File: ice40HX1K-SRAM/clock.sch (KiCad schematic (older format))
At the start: 12 parts

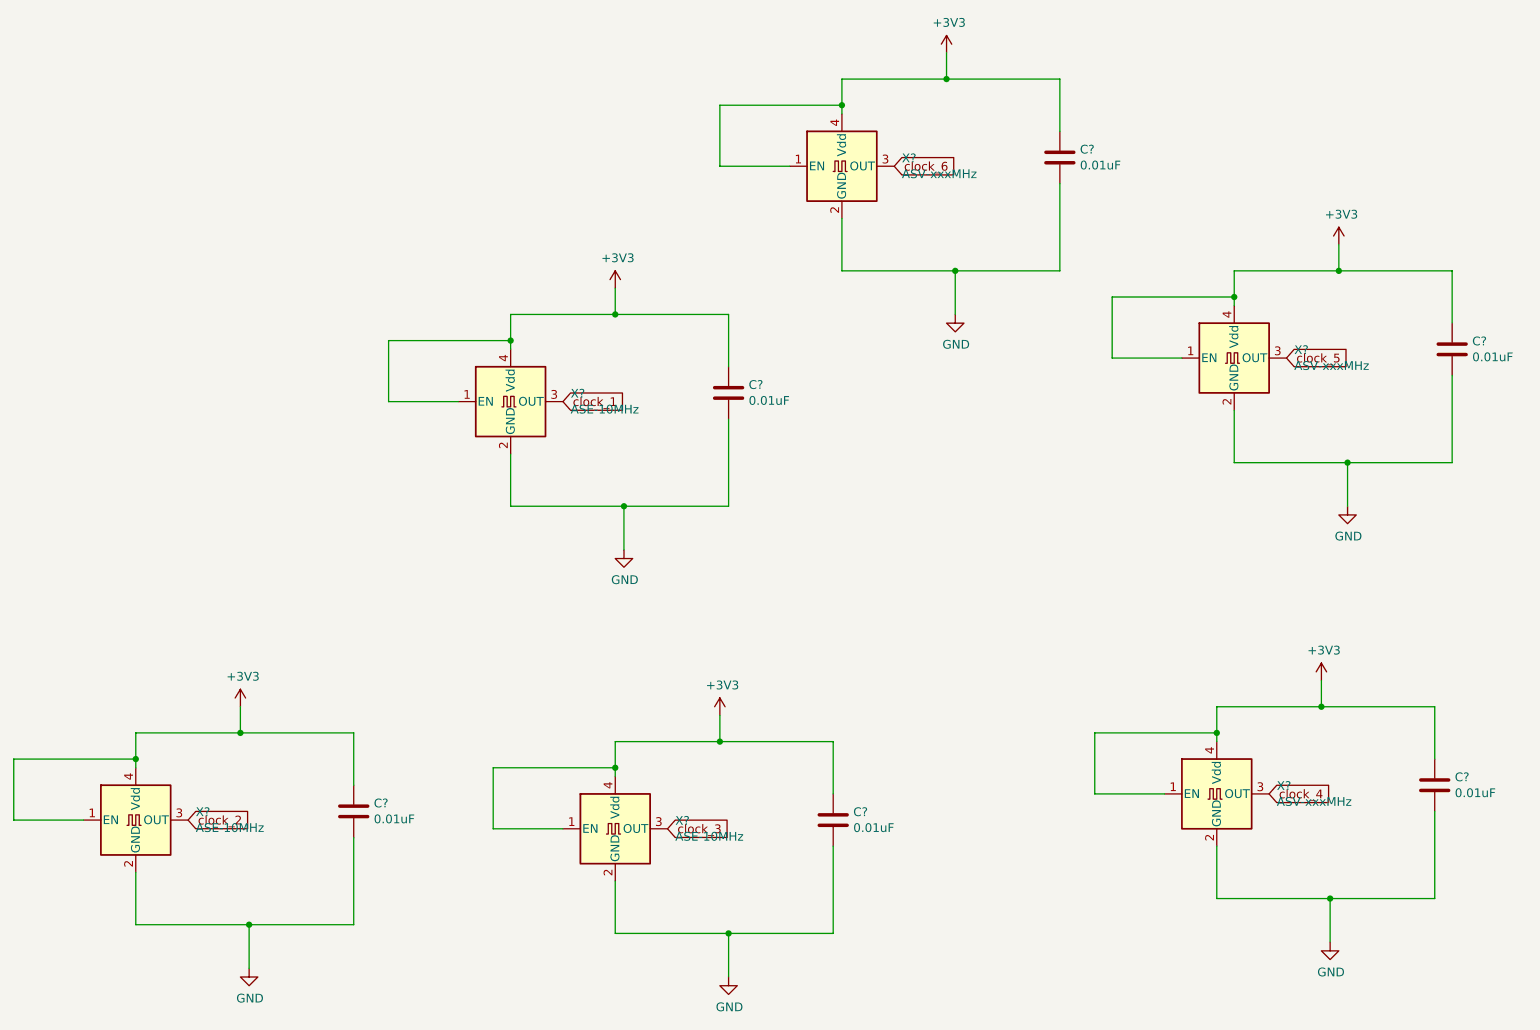
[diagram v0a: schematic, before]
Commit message: wiring FPGA nRF52 and ATSAMD11
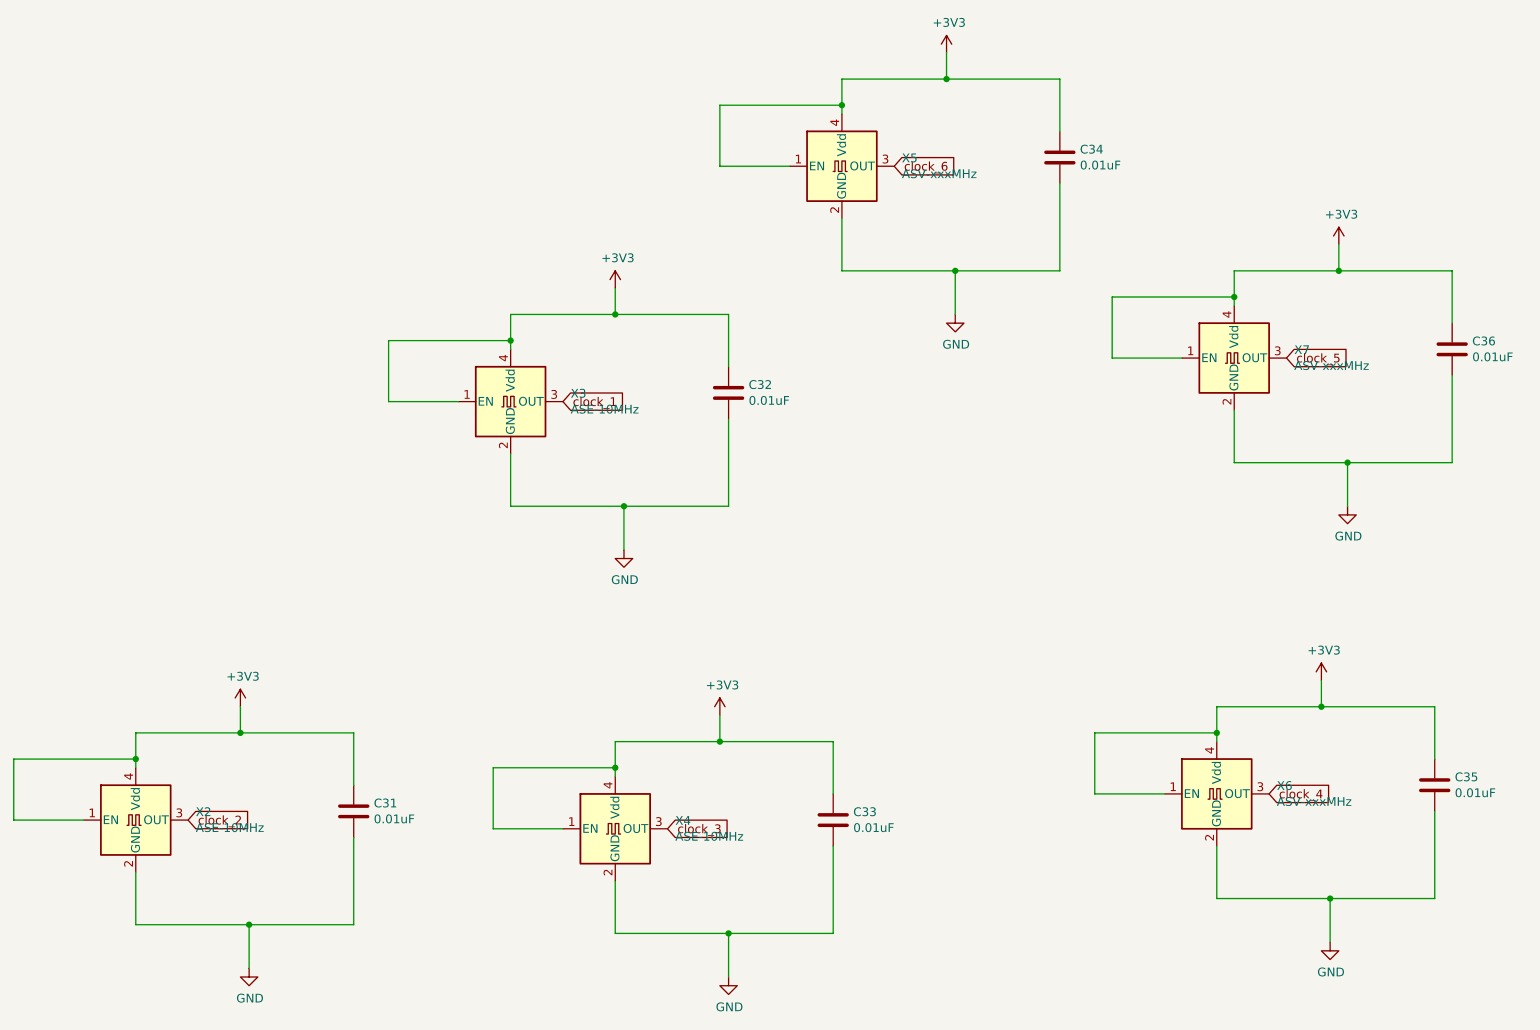
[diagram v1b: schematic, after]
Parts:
- gave numbers to parts that had none: 12
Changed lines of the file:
@@
 $EndDescr
 $Comp
-L Oscillator:ASE-xxxMHz X?
+L Oscillator:ASE-xxxMHz X3
 U 1 1 5E66FD40
 P 4050 2900
-F 0 "X?" H 4394 2946 50  0000 L CNN
+F 0 "X3" H 4394 2946 50  0000 L CNN
 F 1 "ASE-10MHz" H 4394 2855 50  0000 L CNN
 F 2 "Oscillator:Oscillator_SMD_Abracon_ASE-4Pin_3.2x2.5mm" H 4750 2550 50  0001 C CNN
@@
 $EndComp
 $Comp
-L Device:C C?
+L Device:C C32
 U 1 1 5E67058E
 P 5300 2850
-F 0 "C?" H 5415 2896 50  0000 L CNN
+F 0 "C32" H 5415 2896 50  0000 L CNN
 F 1 "0.01uF" H 5415 2805 50  0000 L CNN
 F 2 "" H 5338 2700 50  0001 C CNN
@@
 	5300 3500 5300 3000
 $Comp
-L power:+3V3 #PWR?
+L power:+3V3 #PWR072
 U 1 1 5E670EA7
 P 4650 2250
-F 0 "#PWR?" H 4650 2100 50  0001 C CNN
+F 0 "#PWR072" H 4650 2100 50  0001 C CNN
 F 1 "+3V3" H 4665 2423 50  0000 C CNN
 F 2 "" H 4650 2250 50  0001 C CNN
@@
 $EndComp
 $Comp
-L power:GND #PWR?
+L power:GND #PWR073
 U 1 1 5E67178D
 P 4700 3750
-F 0 "#PWR?" H 4700 3500 50  0001 C CNN
+F 0 "#PWR073" H 4700 3500 50  0001 C CNN
 F 1 "GND" H 4705 3577 50  0000 C CNN
 F 2 "" H 4700 3750 50  0001 C CNN
@@
 clock_1
 $Comp
-L Oscillator:ASV-xxxMHz X?
+L Oscillator:ASV-xxxMHz X7
 U 1 1 5E6438F8
 P 8200 2650
-F 0 "X?" H 8544 2696 50  0000 L CNN
+F 0 "X7" H 8544 2696 50  0000 L CNN
 F 1 "ASV-xxxMHz" H 8544 2605 50  0000 L CNN
 F 2 "Oscillator:Oscillator_SMD_Abracon_ASV-4Pin_7.0x5.1mm" H 8900 2300 50  0001 C CNN
@@
 $EndComp
 $Comp
-L Oscillator:ASE-xxxMHz X?
+L Oscillator:ASE-xxxMHz X2
 U 1 1 5E646F30
 P 1900 5300
-F 0 "X?" H 2244 5346 50  0000 L CNN
+F 0 "X2" H 2244 5346 50  0000 L CNN
 F 1 "ASE-10MHz" H 2244 5255 50  0000 L CNN
 F 2 "Oscillator:Oscillator_SMD_Abracon_ASE-4Pin_3.2x2.5mm" H 2600 4950 50  0001 C CNN
@@
 $EndComp
 $Comp
-L Device:C C?
+L Device:C C31
 U 1 1 5E646F36
 P 3150 5250
-F 0 "C?" H 3265 5296 50  0000 L CNN
+F 0 "C31" H 3265 5296 50  0000 L CNN
 F 1 "0.01uF" H 3265 5205 50  0000 L CNN
 F 2 "" H 3188 5100 50  0001 C CNN
@@
 	3150 5900 3150 5400
 $Comp
-L power:+3V3 #PWR?
+L power:+3V3 #PWR070
 U 1 1 5E646F42
 P 2500 4650
-F 0 "#PWR?" H 2500 4500 50  0001 C CNN
+F 0 "#PWR070" H 2500 4500 50  0001 C CNN
 F 1 "+3V3" H 2515 4823 50  0000 C CNN
 F 2 "" H 2500 4650 50  0001 C CNN
@@
 $EndComp
 $Comp
-L power:GND #PWR?
+L power:GND #PWR071
 U 1 1 5E646F48
 P 2550 6150
-F 0 "#PWR?" H 2550 5900 50  0001 C CNN
+F 0 "#PWR071" H 2550 5900 50  0001 C CNN
 F 1 "GND" H 2555 5977 50  0000 C CNN
 F 2 "" H 2550 6150 50  0001 C CNN
@@
 clock_2
 $Comp
-L Oscillator:ASE-xxxMHz X?
+L Oscillator:ASE-xxxMHz X4
 U 1 1 5E647806
 P 4650 5350
-F 0 "X?" H 4994 5396 50  0000 L CNN
+F 0 "X4" H 4994 5396 50  0000 L CNN
 F 1 "ASE-10MHz" H 4994 5305 50  0000 L CNN
 F 2 "Oscillator:Oscillator_SMD_Abracon_ASE-4Pin_3.2x2.5mm" H 5350 5000 50  0001 C CNN
@@
 $EndComp
 $Comp
-L Device:C C?
+L Device:C C33
 U 1 1 5E64780C
 P 5900 5300
-F 0 "C?" H 6015 5346 50  0000 L CNN
+F 0 "C33" H 6015 5346 50  0000 L CNN
 F 1 "0.01uF" H 6015 5255 50  0000 L CNN
 F 2 "" H 5938 5150 50  0001 C CNN
@@
 	5900 5950 5900 5450
 $Comp
-L power:+3V3 #PWR?
+L power:+3V3 #PWR074
 U 1 1 5E647818
 P 5250 4700
-F 0 "#PWR?" H 5250 4550 50  0001 C CNN
+F 0 "#PWR074" H 5250 4550 50  0001 C CNN
 F 1 "+3V3" H 5265 4873 50  0000 C CNN
 F 2 "" H 5250 4700 50  0001 C CNN
@@
 $EndComp
 $Comp
-L power:GND #PWR?
+L power:GND #PWR075
 U 1 1 5E64781E
 P 5300 6200
-F 0 "#PWR?" H 5300 5950 50  0001 C CNN
+F 0 "#PWR075" H 5300 5950 50  0001 C CNN
 F 1 "GND" H 5305 6027 50  0000 C CNN
 F 2 "" H 5300 6200 50  0001 C CNN
@@
 clock_3
 $Comp
-L Device:C C?
+L Device:C C36
 U 1 1 5E6489E3
 P 9450 2600
-F 0 "C?" H 9565 2646 50  0000 L CNN
+F 0 "C36" H 9565 2646 50  0000 L CNN
 F 1 "0.01uF" H 9565 2555 50  0000 L CNN
 F 2 "" H 9488 2450 50  0001 C CNN
@@
 	9450 3250 9450 2750
 $Comp
-L power:+3V3 #PWR?
+L power:+3V3 #PWR080
 U 1 1 5E6489EF
 P 8800 2000
-F 0 "#PWR?" H 8800 1850 50  0001 C CNN
+F 0 "#PWR080" H 8800 1850 50  0001 C CNN
 F 1 "+3V3" H 8815 2173 50  0000 C CNN
 F 2 "" H 8800 2000 50  0001 C CNN
@@
 $EndComp
 $Comp
-L power:GND #PWR?
+L power:GND #PWR081
 U 1 1 5E6489F5
 P 8850 3500
-F 0 "#PWR?" H 8850 3250 50  0001 C CNN
+F 0 "#PWR081" H 8850 3250 50  0001 C CNN
 F 1 "GND" H 8855 3327 50  0000 C CNN
 F 2 "" H 8850 3500 50  0001 C CNN
@@
 clock_5
 $Comp
-L Oscillator:ASV-xxxMHz X?
+L Oscillator:ASV-xxxMHz X6
 U 1 1 5E64DEA5
 P 8100 5150
-F 0 "X?" H 8444 5196 50  0000 L CNN
+F 0 "X6" H 8444 5196 50  0000 L CNN
 F 1 "ASV-xxxMHz" H 8444 5105 50  0000 L CNN
 F 2 "Oscillator:Oscillator_SMD_Abracon_ASV-4Pin_7.0x5.1mm" H 8800 4800 50  0001 C CNN
@@
 $EndComp
 $Comp
-L Device:C C?
+L Device:C C35
 U 1 1 5E64DEAB
 P 9350 5100
-F 0 "C?" H 9465 5146 50  0000 L CNN
+F 0 "C35" H 9465 5146 50  0000 L CNN
 F 1 "0.01uF" H 9465 5055 50  0000 L CNN
 F 2 "" H 9388 4950 50  0001 C CNN
@@
 	9350 5750 9350 5250
 $Comp
-L power:+3V3 #PWR?
+L power:+3V3 #PWR078
 U 1 1 5E64DEB7
 P 8700 4500
-F 0 "#PWR?" H 8700 4350 50  0001 C CNN
+F 0 "#PWR078" H 8700 4350 50  0001 C CNN
 F 1 "+3V3" H 8715 4673 50  0000 C CNN
 F 2 "" H 8700 4500 50  0001 C CNN
@@
 $EndComp
 $Comp
-L power:GND #PWR?
+L power:GND #PWR079
 U 1 1 5E64DEBD
 P 8750 6000
-F 0 "#PWR?" H 8750 5750 50  0001 C CNN
+F 0 "#PWR079" H 8750 5750 50  0001 C CNN
 F 1 "GND" H 8755 5827 50  0000 C CNN
 F 2 "" H 8750 6000 50  0001 C CNN
@@
 clock_4
 $Comp
-L Oscillator:ASV-xxxMHz X?
+L Oscillator:ASV-xxxMHz X5
 U 1 1 5E64FFD0
 P 5950 1550
-F 0 "X?" H 6294 1596 50  0000 L CNN
+F 0 "X5" H 6294 1596 50  0000 L CNN
 F 1 "ASV-xxxMHz" H 6294 1505 50  0000 L CNN
 F 2 "Oscillator:Oscillator_SMD_Abracon_ASV-4Pin_7.0x5.1mm" H 6650 1200 50  0001 C CNN
@@
 $EndComp
 $Comp
-L Device:C C?
+L Device:C C34
 U 1 1 5E64FFD6
 P 7200 1500
-F 0 "C?" H 7315 1546 50  0000 L CNN
+F 0 "C34" H 7315 1546 50  0000 L CNN
 F 1 "0.01uF" H 7315 1455 50  0000 L CNN
 F 2 "" H 7238 1350 50  0001 C CNN
@@
 	7200 2150 7200 1650
 $Comp
-L power:+3V3 #PWR?
+L power:+3V3 #PWR076
 U 1 1 5E64FFE2
 P 6550 900
-F 0 "#PWR?" H 6550 750 50  0001 C CNN
+F 0 "#PWR076" H 6550 750 50  0001 C CNN
 F 1 "+3V3" H 6565 1073 50  0000 C CNN
 F 2 "" H 6550 900 50  0001 C CNN
@@
 $EndComp
 $Comp
-L power:GND #PWR?
+L power:GND #PWR077
 U 1 1 5E64FFE8
 P 6600 2400
-F 0 "#PWR?" H 6600 2150 50  0001 C CNN
+F 0 "#PWR077" H 6600 2150 50  0001 C CNN
 F 1 "GND" H 6605 2227 50  0000 C CNN
 F 2 "" H 6600 2400 50  0001 C CNN

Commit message: wiring FPGA
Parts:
- C31, C32, C33, C34, C35, C36: footprint (none) -> Capacitor_SMD:C_0402_1005Metric
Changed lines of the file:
@@
 F 0 "C32" H 5415 2896 50  0000 L CNN
 F 1 "0.01uF" H 5415 2805 50  0000 L CNN
-F 2 "" H 5338 2700 50  0001 C CNN
+F 2 "Capacitor_SMD:C_0402_1005Metric" H 5338 2700 50  0001 C CNN
 F 3 "~" H 5300 2850 50  0001 C CNN
 	1    5300 2850
@@
 F 0 "C31" H 3265 5296 50  0000 L CNN
 F 1 "0.01uF" H 3265 5205 50  0000 L CNN
-F 2 "" H 3188 5100 50  0001 C CNN
+F 2 "Capacitor_SMD:C_0402_1005Metric" H 3188 5100 50  0001 C CNN
 F 3 "~" H 3150 5250 50  0001 C CNN
 	1    3150 5250
@@
 F 0 "C33" H 6015 5346 50  0000 L CNN
 F 1 "0.01uF" H 6015 5255 50  0000 L CNN
-F 2 "" H 5938 5150 50  0001 C CNN
+F 2 "Capacitor_SMD:C_0402_1005Metric" H 5938 5150 50  0001 C CNN
 F 3 "~" H 5900 5300 50  0001 C CNN
 	1    5900 5300
@@
 F 0 "C36" H 9565 2646 50  0000 L CNN
 F 1 "0.01uF" H 9565 2555 50  0000 L CNN
-F 2 "" H 9488 2450 50  0001 C CNN
+F 2 "Capacitor_SMD:C_0402_1005Metric" H 9488 2450 50  0001 C CNN
 F 3 "~" H 9450 2600 50  0001 C CNN
 	1    9450 2600
@@
 F 0 "C35" H 9465 5146 50  0000 L CNN
 F 1 "0.01uF" H 9465 5055 50  0000 L CNN
-F 2 "" H 9388 4950 50  0001 C CNN
+F 2 "Capacitor_SMD:C_0402_1005Metric" H 9388 4950 50  0001 C CNN
 F 3 "~" H 9350 5100 50  0001 C CNN
 	1    9350 5100
@@
 F 0 "C34" H 7315 1546 50  0000 L CNN
 F 1 "0.01uF" H 7315 1455 50  0000 L CNN
-F 2 "" H 7238 1350 50  0001 C CNN
+F 2 "Capacitor_SMD:C_0402_1005Metric" H 7238 1350 50  0001 C CNN
 F 3 "~" H 7200 1500 50  0001 C CNN
 	1    7200 1500
